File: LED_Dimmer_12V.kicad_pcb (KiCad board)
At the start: 2 copper layers, 37.5 x 20.3 mm, 10 parts, among them IC1 NE555, T1 IRF610

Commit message: Added a missing trace
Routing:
- net Net-(CONN1-Pad1): track 27.5 -> 39.4 mm
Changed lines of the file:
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@@
   (general
     (links 19)
-    (no_connects 4)
+    (no_connects 1)
     (area 199.314999 109.779999 236.930001 130.250001)
     (thickness 1.6)
     (drawings 5)
-    (tracks 33)
+    (tracks 35)
     (zones 0)
     (modules 10)
@@
   (segment (start 211.725 126.095) (end 211.725 127.635) (width 0.25) (layer F.Cu) (net 3))
   (segment (start 212.725 123.825) (end 212.725 125.095) (width 0.25) (layer F.Cu) (net 3))
+  (segment (start 212.725 116.205) (end 213.995 114.935) (width 0.25) (layer B.Cu) (net 4))
+  (segment (start 213.995 114.935) (end 224.155 114.935) (width 0.25) (layer B.Cu) (net 4))
   (segment (start 221.615 114.935) (end 219.075 112.395) (width 0.25) (layer F.Cu) (net 4))
   (segment (start 219.075 112.395) (end 217.17 112.395) (width 0.25) (layer F.Cu) (net 4))

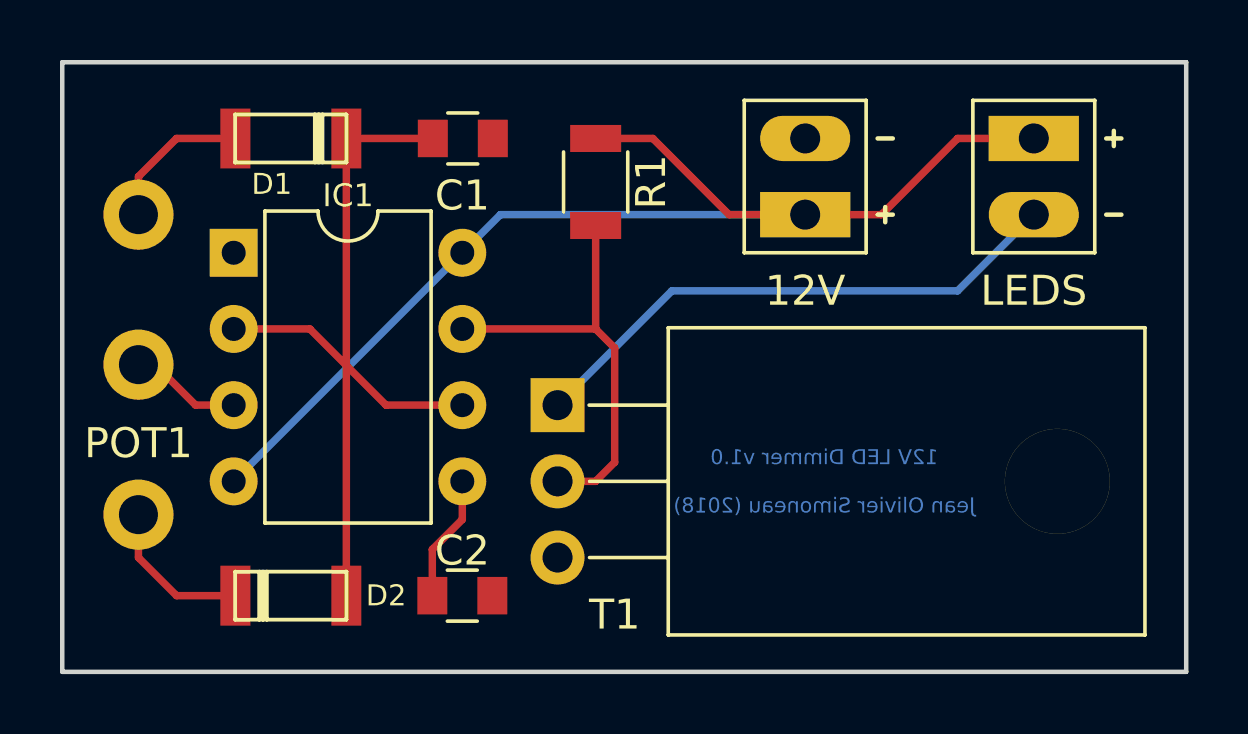
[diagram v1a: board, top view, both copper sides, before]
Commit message: Corrected IRF610 footprint (swapped G and D; pads 1&2)
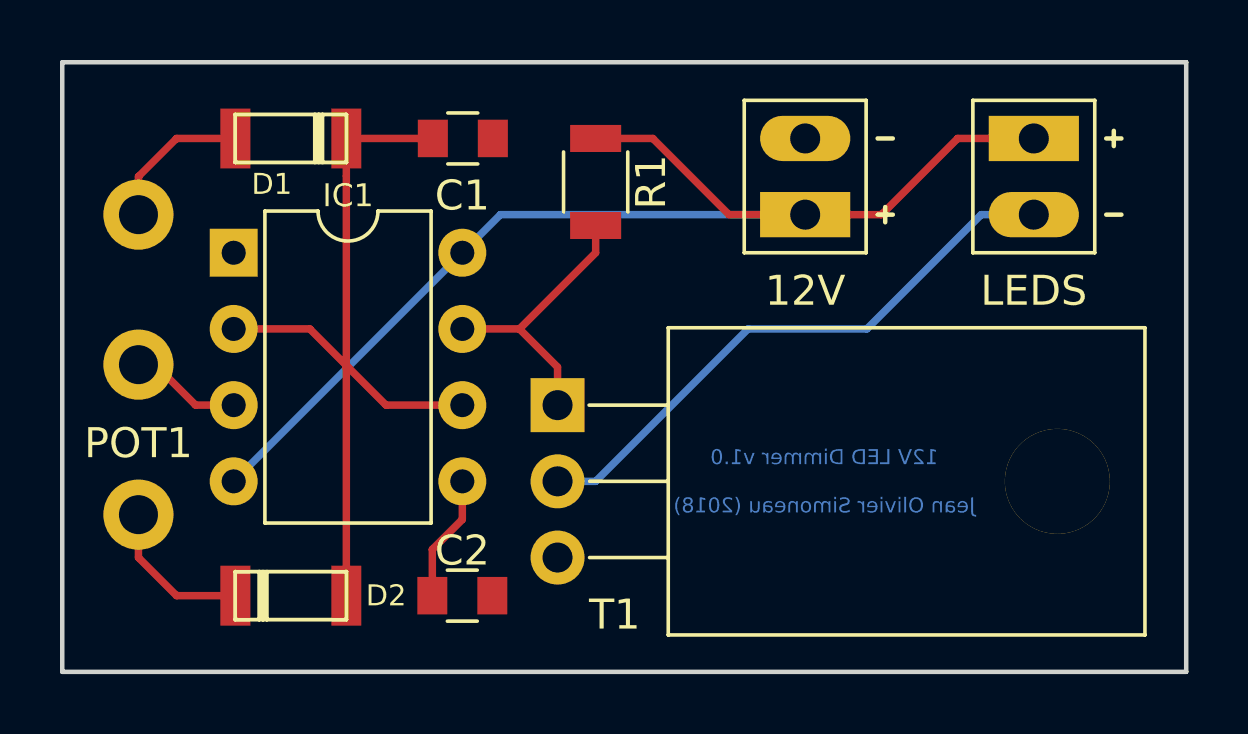
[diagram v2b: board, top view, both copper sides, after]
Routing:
- net Net-(IC1-Pad7): track 14.8 -> 9.47 mm
- net Net-(LS1-Pad1): track 18.5 -> 19.6 mm

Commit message: v1.2, THT footprints for R1 and Cs. Updated README with 3D render and picture of first populated PCB.
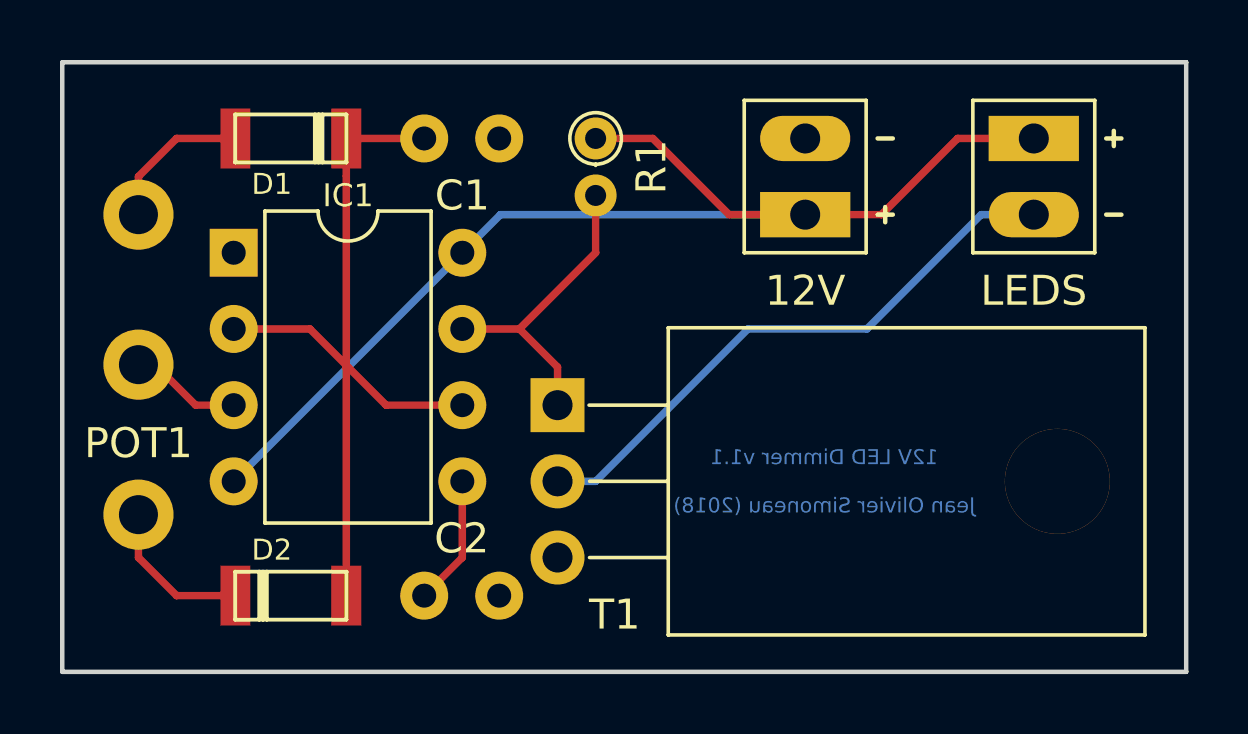
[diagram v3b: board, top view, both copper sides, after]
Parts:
- C1: value 0.1µF -> 10nF; footprint Capacitors_SMD:C_0805 -> Capacitors_THT:C_Disc_D5.0mm_W2.5mm_P2.50mm
- C2: footprint Capacitors_SMD:C_0805 -> Capacitors_THT:C_Disc_D5.0mm_W2.5mm_P2.50mm
- R1: footprint Resistors_SMD:R_1206 -> Resistors_THT:R_Axial_DIN0204_L3.6mm_D1.6mm_P1.90mm_Vertical
- moved R1 1.45 mm to (217.2, 112.4)
- moved C1 1.29 mm to (211.5, 112.4)
- moved C2 1.27 mm to (211.5, 127.6)
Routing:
- net Net-(IC1-Pad7): track 9.47 -> 10.5 mm
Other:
- board text added: "12V LED Dimmer v1.1 Jean Olivier Simoneau (2018)"
- board text removed: "12V LED Dimmer v1.0 Jean Olivier Simoneau (2018)"
